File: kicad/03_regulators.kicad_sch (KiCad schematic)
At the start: 0 parts

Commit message: Phase 1: sheet 3 (regulators) transcribed; centred field text for two-pin parts
Co-Authored-By: Claude Fable 5.1 <noreply@anthropic.com>
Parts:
- added C16, C40, C5, C6: 1u, symbol ac_psu:C
- added C3, C4, C69, C70: 100n, symbol ac_psu:C
- added R19, R32: 420R, symbol ac_psu:R
- added R30, R40: 820R, symbol ac_psu:R
- added REF1, REF2: REF3025, symbol ac_psu:REF3025
- added U10, U3: TPS73033DBVT, symbol ac_psu:TPS73033DBVT
- added U8: VXO7805-1000, symbol ac_psu:VXO7805-1000
- added U9: VXO7805-500, symbol ac_psu:VXO7805-500
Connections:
- new net: C6.2, R32.1, REF2.3 (VOUT)
- new net: C40.2, R19.1, REF1.3 (VOUT)
- new net 20V: U9.1 (+VIN)
- new net 20V_ISO_SEC: U8.1 (+VIN)
- new net 3V3_ISO: C3.2, C5.2, REF2.2 (VIN), U10.5 (OUT)
- new net 5V: C70.2, U3.1 (IN), U3.3 (EN), U9.3 (+VOUT/GND)
- new net 5V_ISOL: C4.2, U10.1 (IN), U10.3 (EN), U8.3 (+VOUT)
- new net GND: C16.1, C40.1, C69.1, C70.1, R30.2, REF1.1 (GND), U3.2 (GND), U9.2 (GND/-VOUT)
- new net ISOGND: C3.1, C4.1, C5.1, C6.1, R40.2, REF2.1 (GND), U10.2 (GND), U8.2 (GND)
- new net REF_1V65: R19.2, R30.1
- new net REF_1V65_ISO: R32.2, R40.1
- new net VCC: C16.2, C69.2, REF1.2 (VIN), U3.5 (OUT)
- no-connect marks 0 -> 2
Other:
- note added: "3V3 / 3v3 in the Proteus schematic = net VCC (VCC/VDD=POWER); 3V3_ISO is the isolated 3.3 V."
- note added: "REF3025 pin ids follow Proteus (1=GND 2=VIN 3=VOUT), not the TI datasheet - see STATUS.md."

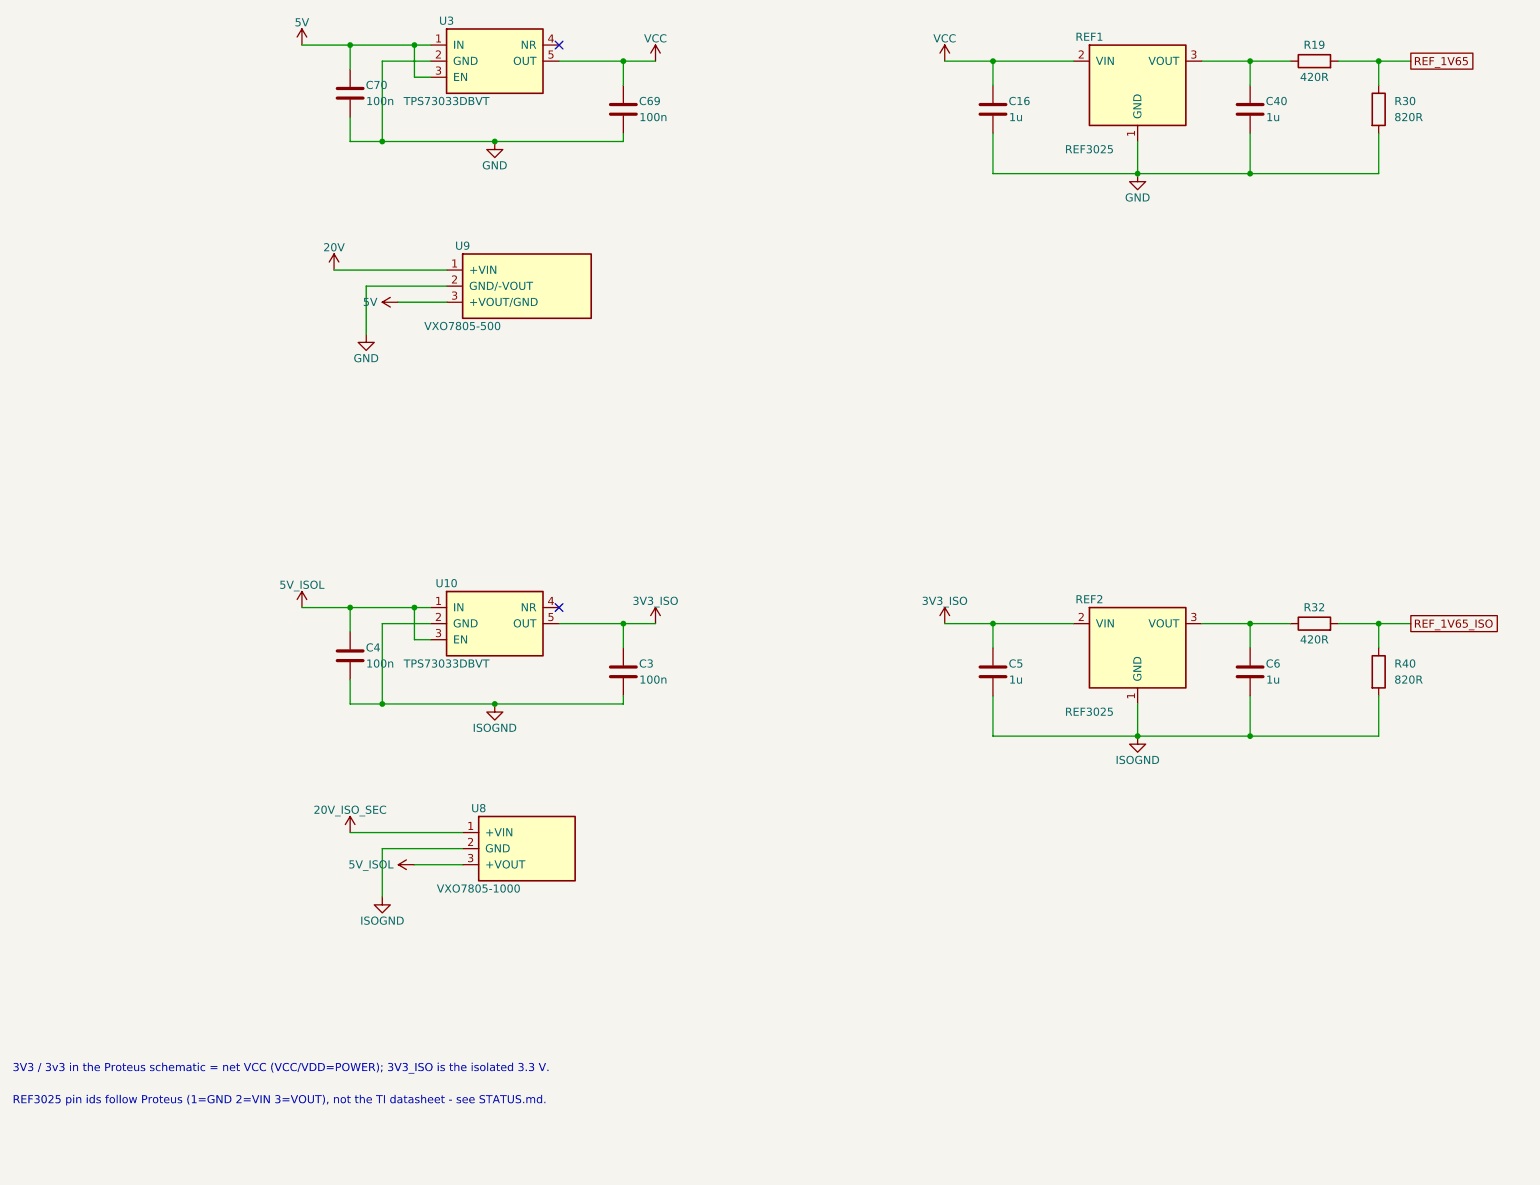
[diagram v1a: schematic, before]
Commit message: Phase 1: sheet 11 (signal isolators); builder: rotation-aware fields, text sides, terminals
Co-Authored-By: Claude Fable 5.1 <noreply@anthropic.com>
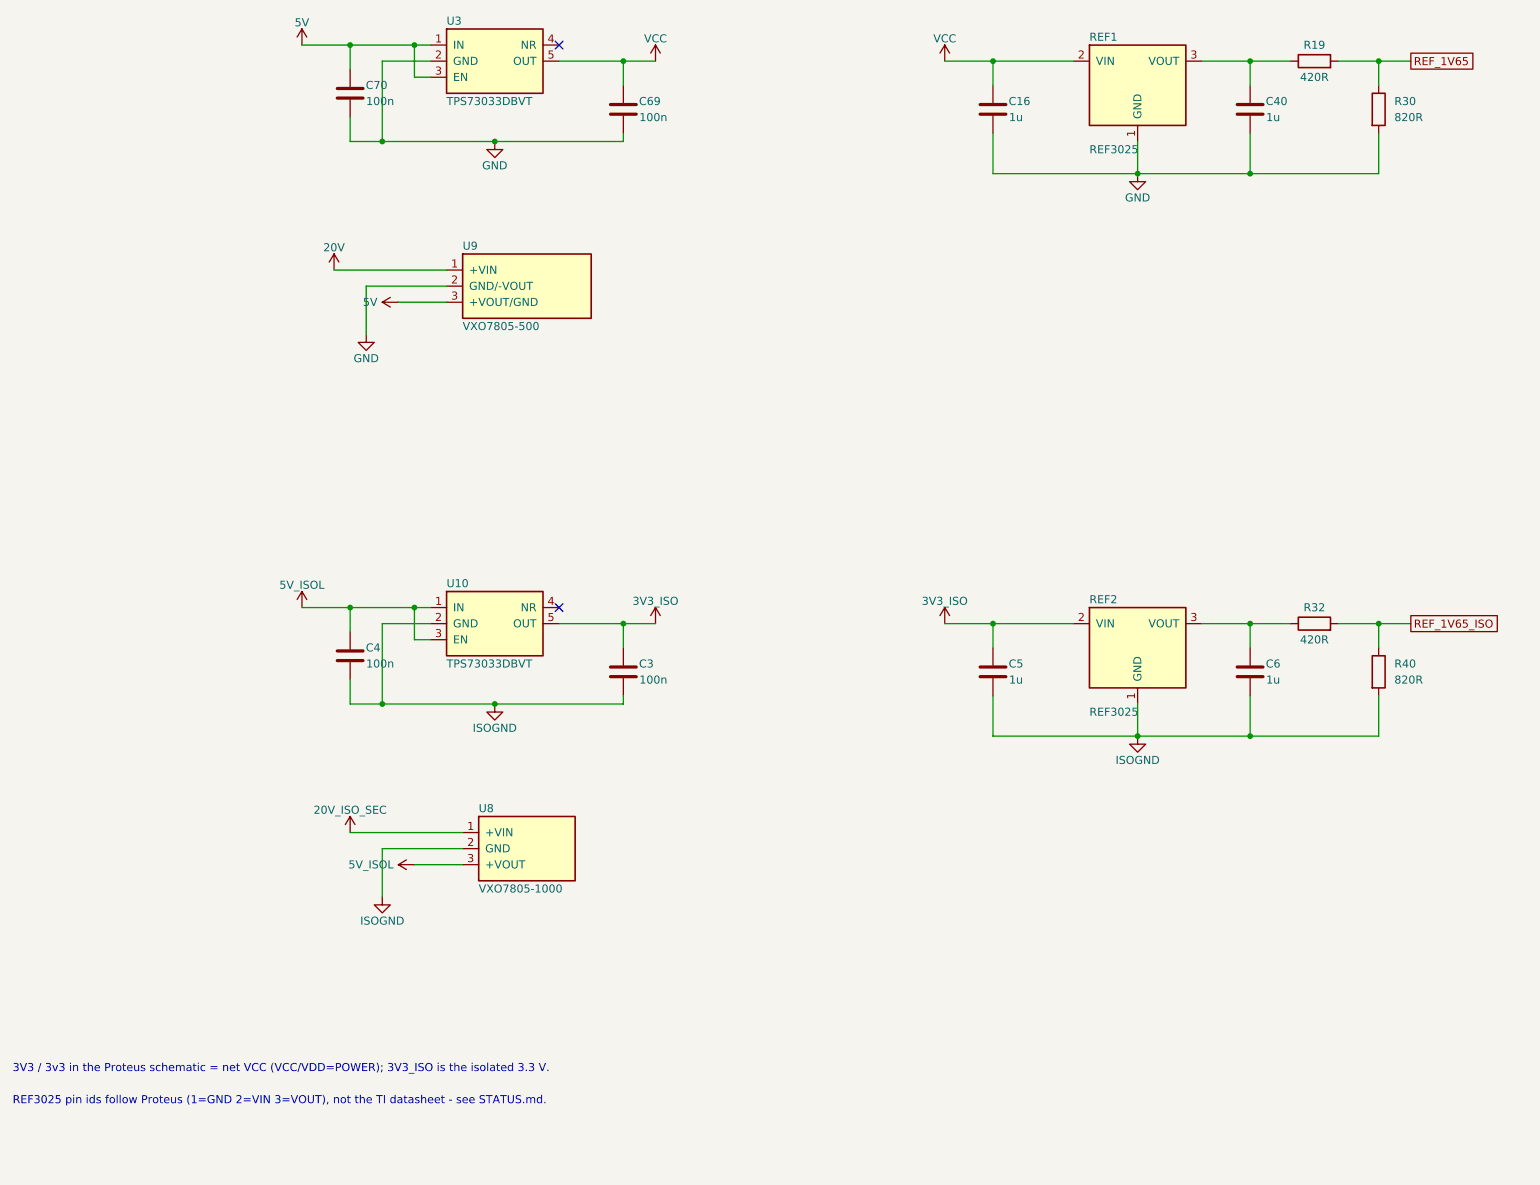
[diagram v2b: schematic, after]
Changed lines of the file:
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@@
 					(size 1.27 1.27)
 				)
+				(justify left)
 			)
 		)
@@
 					(size 1.27 1.27)
 				)
+				(justify left)
 			)
 		)
@@
 					(size 1.27 1.27)
 				)
+				(justify left)
 			)
 		)
@@
 					(size 1.27 1.27)
 				)
+				(justify left)
 			)
 		)
@@
 					(size 1.27 1.27)
 				)
+				(justify left)
 			)
 		)
@@
 					(size 1.27 1.27)
 				)
+				(justify left)
 			)
 		)
@@
 					(size 1.27 1.27)
 				)
+				(justify left)
 			)
 		)
@@
 					(size 1.27 1.27)
 				)
+				(justify left)
 			)
 		)
@@
 					(size 1.27 1.27)
 				)
+				(justify left)
 			)
 		)
@@
 					(size 1.27 1.27)
 				)
+				(justify left)
 			)
 		)
@@
 					(size 1.27 1.27)
 				)
+				(justify left)
 			)
 		)
@@
 					(size 1.27 1.27)
 				)
-			)
-		)
+				(justify left)
+			)
+		)

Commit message: Phase 2 done: footprints assigned and verified against IPC pads
- tools/gen_footprints.py -> lib/footprint_map.csv + lib/ac_psu.pretty (20 project footprints)
- tools/fpgeom.py: footprint pad loader and rigid fit; tools/check_footprints.py (+ pcbnew
  placement check), added to check_all.sh; reports/footprint_fit.csv for Phase 3 placement
- sch_builder: Footprint field from the map, deterministic UUIDs; all sheets regenerated
- kicad/fp-lib-table; STATUS.md (decisions, residuals, REF3025/C67 findings); Phase 3 prompt

Co-Authored-By: Claude Opus 5.5 <noreply@anthropic.com>
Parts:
- C16, C3, C4, C40, C5, C6, C69, C70: footprint (none) -> Capacitor_SMD:C_0402_1005Metric
- R19, R30, R32, R40: footprint (none) -> Resistor_SMD:R_0402_1005Metric
- REF1, REF2: footprint (none) -> ac_psu:SOT-23_Proteus
- U10, U3: footprint (none) -> ac_psu:SOT-23-5_TPS73033
- U8, U9: footprint (none) -> Converter_DCDC:Converter_DCDC_RECOM_R-78E-0.5_THT
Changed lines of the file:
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@@
 			)
 		)
-		(property "Footprint" ""
+		(property "Footprint" "ac_psu:SOT-23-5_TPS73033"
 			(at 101.6 50.8 0)
 			(effects
@@
 			)
 		)
-		(property "Footprint" ""
+		(property "Footprint" "Capacitor_SMD:C_0402_1005Metric"
 			(at 77.7748 52.07 0)
 			(effects
@@
 			)
 		)
-		(property "Footprint" ""
+		(property "Footprint" "Capacitor_SMD:C_0402_1005Metric"
 			(at 120.9548 54.61 0)
 			(effects
@@
 			)
 		)
-		(property "Footprint" ""
+		(property "Footprint" "Converter_DCDC:Converter_DCDC_RECOM_R-78E-0.5_THT"
 			(at 106.68 86.36 0)
 			(effects
@@
 			)
 		)
-		(property "Footprint" ""
+		(property "Footprint" "ac_psu:SOT-23_Proteus"
 			(at 203.2 50.8 0)
 			(effects
@@
 			)
 		)
-		(property "Footprint" ""
+		(property "Footprint" "Capacitor_SMD:C_0402_1005Metric"
 			(at 179.3748 54.61 0)
 			(effects
@@
 			)
 		)
-		(property "Footprint" ""
+		(property "Footprint" "Capacitor_SMD:C_0402_1005Metric"
 			(at 220.0148 54.61 0)
 			(effects
@@
 			)
 		)
-		(property "Footprint" ""
+		(property "Footprint" "Resistor_SMD:R_0402_1005Metric"
 			(at 231.14 52.578 0)
 			(effects
@@
 			)
 		)
-		(property "Footprint" ""
+		(property "Footprint" "Resistor_SMD:R_0402_1005Metric"
 			(at 239.522 58.42 0)
 			(effects
@@
 			)
 		)
-		(property "Footprint" ""
+		(property "Footprint" "ac_psu:SOT-23-5_TPS73033"
 			(at 101.6 139.7 0)
 			(effects
@@
 			)
 		)
-		(property "Footprint" ""
+		(property "Footprint" "Capacitor_SMD:C_0402_1005Metric"
 			(at 77.7748 140.97 0)
 			(effects
@@
 			)
 		)
-		(property "Footprint" ""
+		(property "Footprint" "Capacitor_SMD:C_0402_1005Metric"
 			(at 120.9548 143.51 0)
 			(effects
@@
 			)
 		)
-		(property "Footprint" ""
+		(property "Footprint" "Converter_DCDC:Converter_DCDC_RECOM_R-78E-0.5_THT"
 			(at 106.68 175.26 0)
 			(effects
@@
 			)
 		)
-		(property "Footprint" ""
+		(property "Footprint" "ac_psu:SOT-23_Proteus"
 			(at 203.2 139.7 0)
 			(effects
@@
 			)
 		)
-		(property "Footprint" ""
+		(property "Footprint" "Capacitor_SMD:C_0402_1005Metric"
 			(at 179.3748 143.51 0)
 			(effects
@@
 			)
 		)
-		(property "Footprint" ""
+		(property "Footprint" "Capacitor_SMD:C_0402_1005Metric"
 			(at 220.0148 143.51 0)
 			(effects
@@
 			)
 		)
-		(property "Footprint" ""
+		(property "Footprint" "Resistor_SMD:R_0402_1005Metric"
 			(at 231.14 141.478 0)
 			(effects
@@
 			)
 		)
-		(property "Footprint" ""
+		(property "Footprint" "Resistor_SMD:R_0402_1005Metric"
 			(at 239.522 147.32 0)
 			(effects

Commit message: Phase 3 done: PCB rebuilt from the Proteus gerbers with nets and zones
tools/make_pcb.sh regenerates kicad/ac_psu.kicad_pcb (byte-reproducible):
build_pcb.py (footprints with nets and symbol links at the Proteus
positions, outline, mounting holes, rules), gerber_to_tracks.py (4052
tracks, 173 vias; pour edge strokes recognised and skipped),
assign_nets.py (union-find over copper, 0 shorts/orphans/opens with
pours), pours_to_zones.py (79 zones = Proteus pour copper incl. holes).

New checks in check_all.sh: check_board.py (pads/holes/vias vs IPC),
assign_nets.py --check (after zone fill), drc.py (0 shorts, 0
unconnected, 0 parity issues; courtyard overlaps accepted).

Footprints (user decision): Proteus pad sizes for the headers, TSSOP,
SOT-23(-5), SOIC-16W packages whose KiCad pads shorted/violated
clearance; Proteus pads and drills for TO-247, VXO7805, P27.5 film and
snap-in caps; tighter courtyards for IPC-built footprints.

Co-Authored-By: Claude Opus 5.5 <noreply@anthropic.com>
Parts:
- U8, U9: footprint Converter_DCDC:Converter_DCDC_RECOM_R-78E-0.5_THT -> ac_psu:Converter_DCDC_RECOM_R-78E-0.5_THT_Proteus
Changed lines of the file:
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@@
 			)
 		)
-		(property "Footprint" "Converter_DCDC:Converter_DCDC_RECOM_R-78E-0.5_THT"
+		(property "Footprint" "ac_psu:Converter_DCDC_RECOM_R-78E-0.5_THT_Proteus"
 			(at 106.68 86.36 0)
 			(effects
@@
 			)
 		)
-		(property "Footprint" "Converter_DCDC:Converter_DCDC_RECOM_R-78E-0.5_THT"
+		(property "Footprint" "ac_psu:Converter_DCDC_RECOM_R-78E-0.5_THT_Proteus"
 			(at 106.68 175.26 0)
 			(effects

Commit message: v4: R19/R32 422R instead of 420R (not E96, not stocked at JLC), fix 9
2.5 V x 820/(422+820) = 1.6506 V (420R: 1.6532 V). Deviation value rows,
sheet 3 note, board values.

Co-Authored-By: Claude Opus 5.5 <noreply@anthropic.com>
Claude-Session: https://claude.ai/code/session_01Am5hpeWpvZbzmHWspFiWJm
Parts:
- R19, R32: value 420R -> 422R
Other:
- note added: "v4: R19/R32 422R (E96, JLC stock) instead of 420R: 2.5 V x 820/(422+820) = 1.6506 V (420R: 1.6532 V)."
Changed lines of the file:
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@@
 			)
 		)
-		(property "Value" "420R"
+		(property "Value" "422R"
 			(at 231.14 53.34 270)
 			(effects
@@
 			)
 		)
-		(property "Value" "420R"
+		(property "Value" "422R"
 			(at 231.14 142.24 270)
 			(effects
@@
 		(effects
 			(font
+				(size 1.27 1.27)
+			)
+			(justify left bottom)
+		)
+	)
+	(text "v4: R19/R32 422R (E96, JLC stock) instead of 420R: 2.5 V x 820/(422+820) = 1.6506 V (420R: 1.6532 V)."
+		(exclude_from_sim no)
+		(at 25.4 220.98 0)
+		(effects
+			(font

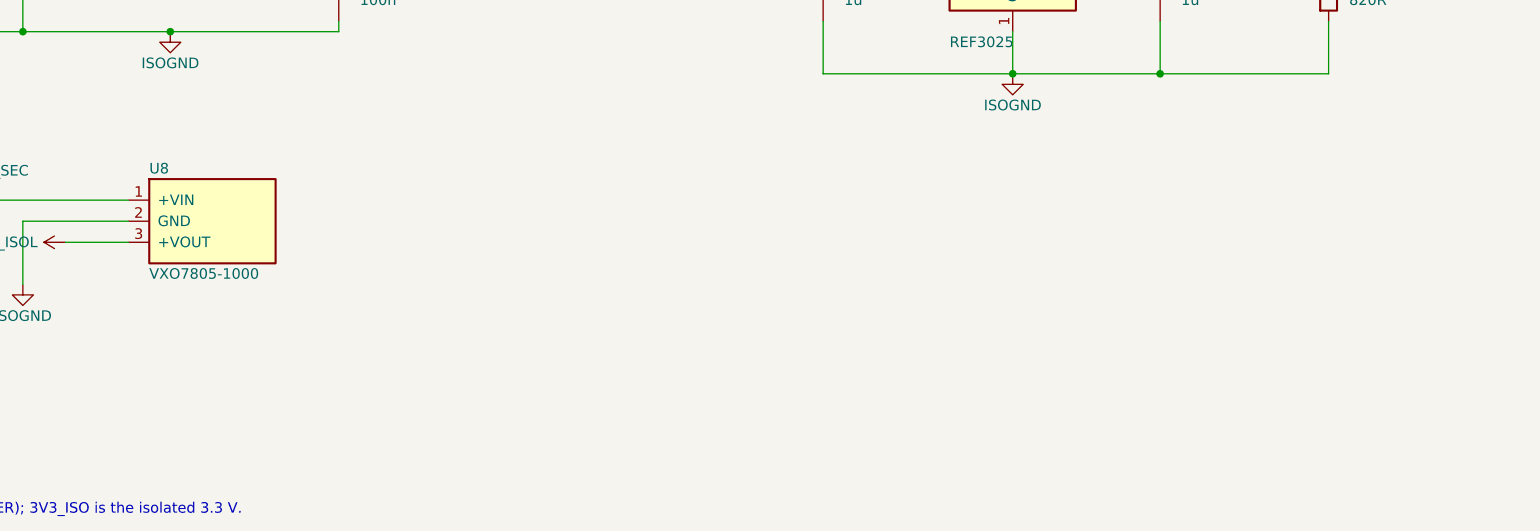
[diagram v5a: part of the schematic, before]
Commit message: v4 fix 10: U8 K7805-2000R3 (5 V / 2 A) with C93/C94 per its datasheet
For the isolated control card (efinix_soc_board POWER_BUDGET.md): U8 value
VXO7805-1000 -> Mornsun K7805-2000R3 (same SIP-3 pinout and footprint, U9
unchanged). C93 10u 50V X7R 1210 (22u 50V not stocked in 1206/1210) at pin 1,
C94 22u 10V 0805 at pin 3, bottom side just south of U8's pins with short
B.Cu tracks; pin 2 is on the In1 ISOGND zone. Deviation rows (value, 2 parts,
4 pins, B.Cu area), sheet 3, part map. Footprint courtyard 0.075 mm short of
the K7805's 6.85 mm body depth (kept, noted).

Co-Authored-By: Claude Opus 5.5 <noreply@anthropic.com>
Claude-Session: https://claude.ai/code/session_01Am5hpeWpvZbzmHWspFiWJm
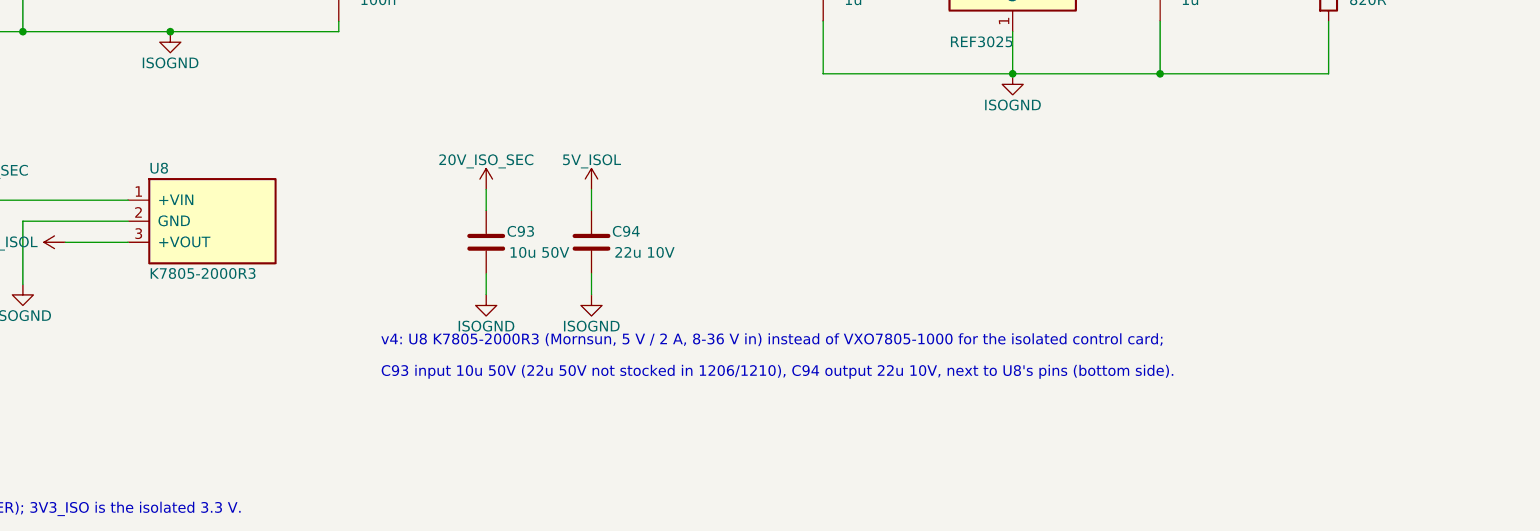
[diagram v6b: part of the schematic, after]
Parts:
- added C93: 10u 50V, Capacitor_SMD:C_1210_3225Metric, symbol ac_psu:C
- added C94: 22u 10V, Capacitor_SMD:C_0805_2012Metric, symbol ac_psu:C
- U8: value VXO7805-1000 -> K7805-2000R3
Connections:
- net 20V_ISO_SEC: now also C93.1
- net 5V_ISOL: now also C94.1
- net ISOGND: now also C93.2, C94.2
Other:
- note added: "C93 input 10u 50V (22u 50V not stocked in 1206/1210), C94 output 22u 10V, next to U8's pins (bottom side)."
- note added: "v4: U8 K7805-2000R3 (Mornsun, 5 V / 2 A, 8-36 V in) instead of VXO7805-1000 for the isolated control card;"
